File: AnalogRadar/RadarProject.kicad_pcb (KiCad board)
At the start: 4 copper layers, 85 x 49 mm, 67 parts, among them J1 Conn_Coaxial, J2 Conn_Coaxial, J3 Conn_01x05, Q1 Q_NPN_BCE, SW1 SW_SPDT, U1 AT0603T03ECATD, U2 PD2328J5050S2HF, U3 BGU8052, U4 BGU8052, U5 CVCO55CC-2230-2430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

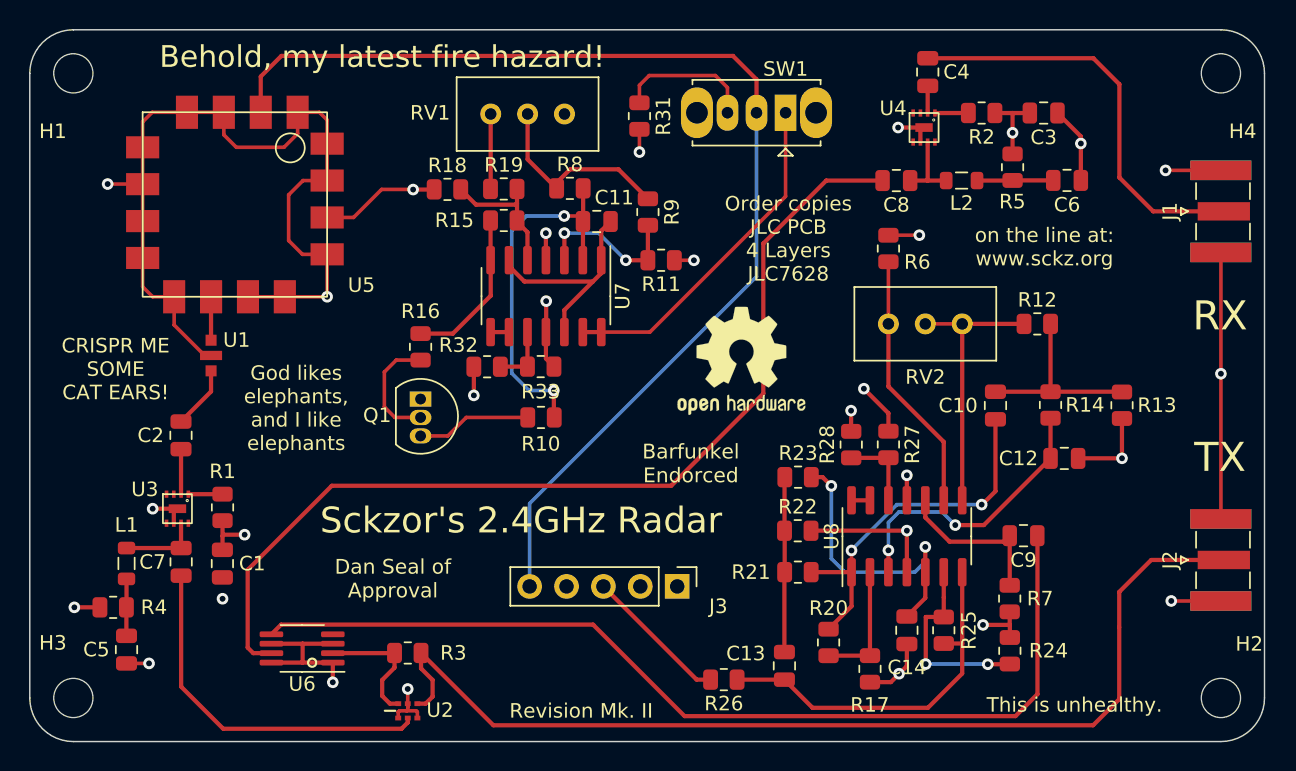
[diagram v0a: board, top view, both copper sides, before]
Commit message: added pico carrier board
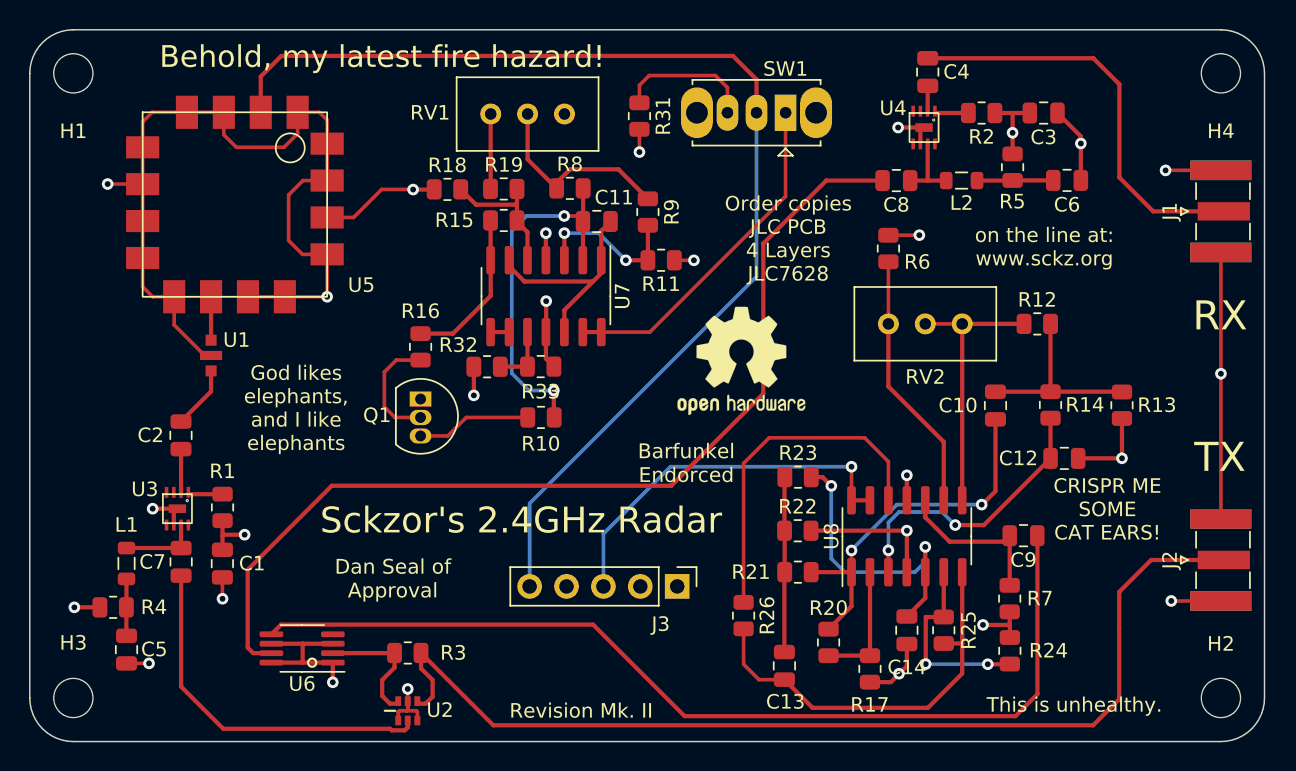
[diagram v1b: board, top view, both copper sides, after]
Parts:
- removed R27, R28: 10k, Resistor_SMD:R_0805_2012Metric
- moved R26 4.61 mm to (69.1, 60.3), turned to 90 degrees
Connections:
- R26 pad 2: Net-(J3-Pad3) -> Net-(R26-Pad2)
- U8 pad 12: Net-(R27-Pad2) -> Net-(R26-Pad2)
- U8 pad 13: Net-(U8-Pad13) -> Net-(J3-Pad3)
- U8 pad 14: Net-(U8-Pad13) -> Net-(J3-Pad3)
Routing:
- net Net-(R26-Pad2): track 0.00 -> 23.6 mm
- net Net-(AE2-Pad2): track 21.8 -> 3.42 mm
- net Net-(AE1-Pad2): track 3.81 -> 22.2 mm
- net Net-(J3-Pad3): track 10.0 -> 26.2 mm, vias 0 -> 1
- net Net-(R27-Pad2): track 5.50 -> 0.00 mm
- net +5V: track 51.7 -> 48.1 mm, vias 12 -> 11
- net Net-(C13-Pad1): track 25.5 -> 28.0 mm
- net Net-(U8-Pad13): track 1.27 -> 0.00 mm
- net Earth: vias 17 -> 16
